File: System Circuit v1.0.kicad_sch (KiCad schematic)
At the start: 260 parts, among them J1 Barrel_Jack_Switch, J10 Conn_01x02, J11 Conn_01x02, J17 MAIN TERMINAL, J18 XT-90F, J19 XT-90F, J2 USB_A, J21 XT-90F, J22 Conn_01x02, J24 XT-90F, J26 Conn_01x02, J27 Conn_01x03, J28 Conn_01x03, J29 Conn_01x03, J3 Screw_Terminal_01x02, J30 Conn_01x03, J31 XT-90F, J32 Conn_01x03, J33 Conn_01x03, J34 XT-90F, J36 XT-90F, J37 Conn_01x02, J4 Jet Term, J40 XT-90F, J41 XT-90F, J43 XT-90F, J44 Conn_01x02, J46 XT-90F, J47 XT-90F, J49 XT-90F, J5 2X2M-NM, J50 Conn_01x02, J51 Drive L1, J53 XT-90F, J54 Drive L2, J55 Drive R1, J56 Drive R2, J57 Conn_01x03, J58 Ex Sprckt, J6 Conn_01x04, J64 Conn_01x03, J65 Conn_01x03, J66 Dep Tilt, J67 Ex DSC/ASC, J68 Ex Tilt, J69 Conn_01x03, J7 ICSP1, J73 Conn_01x03, J74 Conn_01x03, J75 E-Switch, J8 Conn_01x04, J9 Conn_01x02, K1 RT314A12, M1 M1-DRVTRN: L, M10 M2-DRVTRN: LFT, M11 Ex Tilt 2, M12 Ex Dscnd 2, M2 M2-DRVTRN: L, M3 M1-DRVTRN: R, M4 M2-DRVTRN: R, M5 M-EXCV: SPRCKT, M6 Motor_Servo_Hitec, M7 Motor_Servo_Hitec, M8 Ex Tilt 1, M9 Ex Dscnd 1, Q1 PMV48XP, Q2 PNP, Q3 IRF7403, SW1 SW_Push_Dual, SW2 SW_Push_SPDT, SW3 SW_Push_DPDT, SW4 SW_Push_DPDT, U1 LD1117S50TR_SOT223, U10 SABERTOOTH 2X12, U11 LMV358, U12 SABERTOOTH 2X12, U18 SABERTOOTH 2X12, U19 ACS758xCB-050B, U2 LMV358, U20 ACS758xCB-050B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

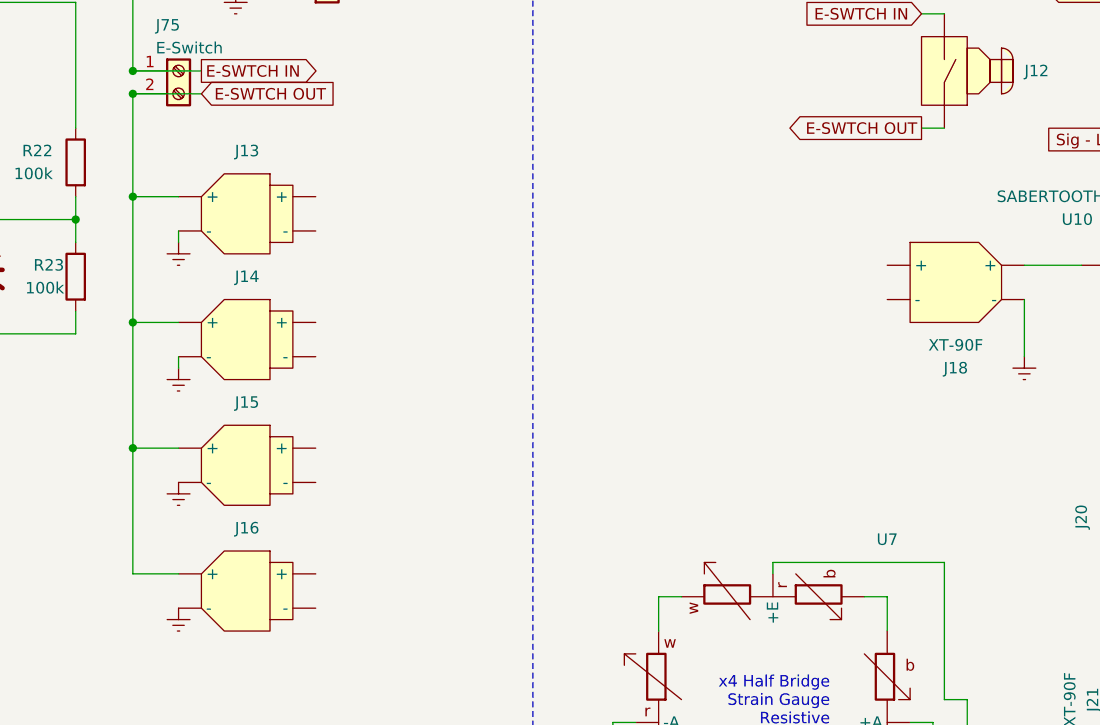
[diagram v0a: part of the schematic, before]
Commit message: created button control code
also changed init_DIR() to 2 separate functs
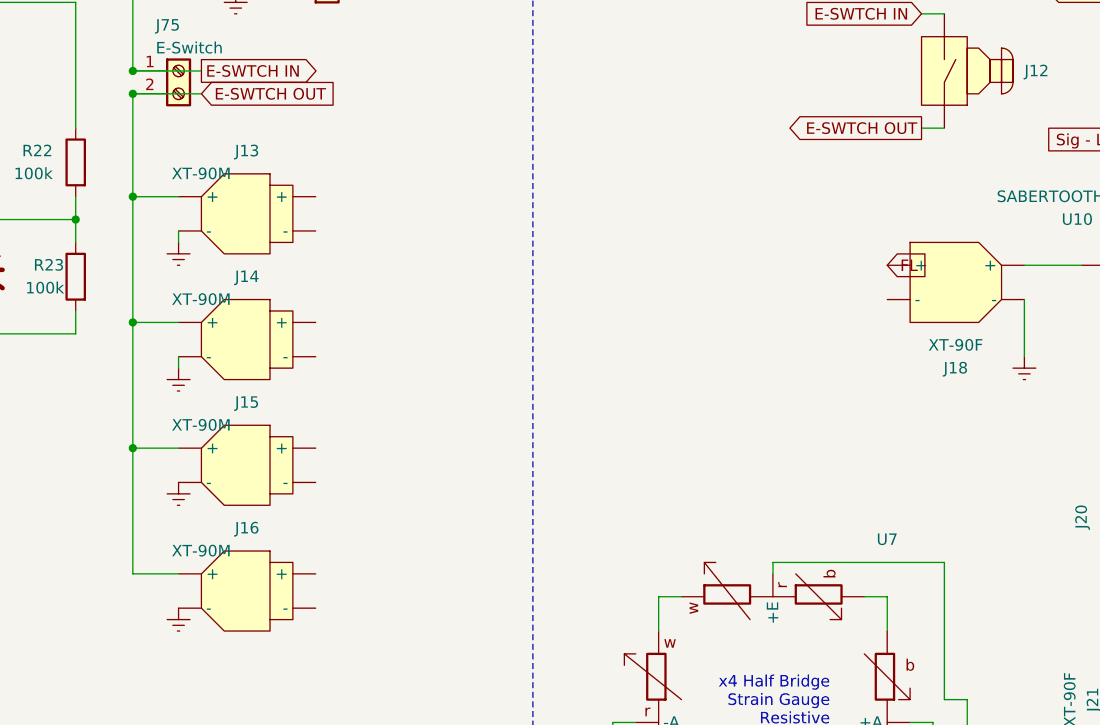
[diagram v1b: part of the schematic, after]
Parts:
- J13, J14, J15, J16: value ~ -> XT-90M
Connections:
- net at J45. (-): now also U18. (S2)
- net at J42. (-): now also U18. (S2)
- net at J38. (-): now also J31. (-); no longer P2. (-)
- net at J52. (-): now also U24. (S2)
- net at J35. (-): no longer U12. (S2)
- net at J39. (-): no longer U12. (S2)
- net at P1. (-): now also J25. (-); no longer J31. (-)
- net FL: now reaches J18. (-)
- net at J25. (-): now also J19. (-); no longer P1. (-)
- net at J48. (-): now also U24. (S2)
- net at J23. (-): now also U10. (S2)
- net at J20. (-): now also U10. (S2)
- new net: J45. (-), U18. (S2)
- new net: J42. (-), U18. (S2)
- new net: J38. (-), P2. (-)
- new net: J52. (-), U24. (S2)
- new net: J35. (-), U12. (S2) (x2)
- new net: J39. (-), U12. (S2) (x2)
- new net: J34. (-), U12. (S2)
- new net: J31. (-), P1. (-) (x2)
- new net: J31. (-), J38. (-)
- new net: J18. (-), U10. (S2)
- new net: J25. (-), P1. (-)
- new net: J19. (-), J25. (-)
- new net: J48. (-), U24. (S2)
- new net: J47. (-), U24. (S2)
- new net: J23. (-), U10. (S2)
- new net: J20. (-), U10. (S2)
- new net: J41. (-), U18. (S2)
- now unconnected: J35. (-), J39. (-)
